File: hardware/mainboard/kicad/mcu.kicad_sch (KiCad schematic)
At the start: 8 parts, among them J15 J_EXP

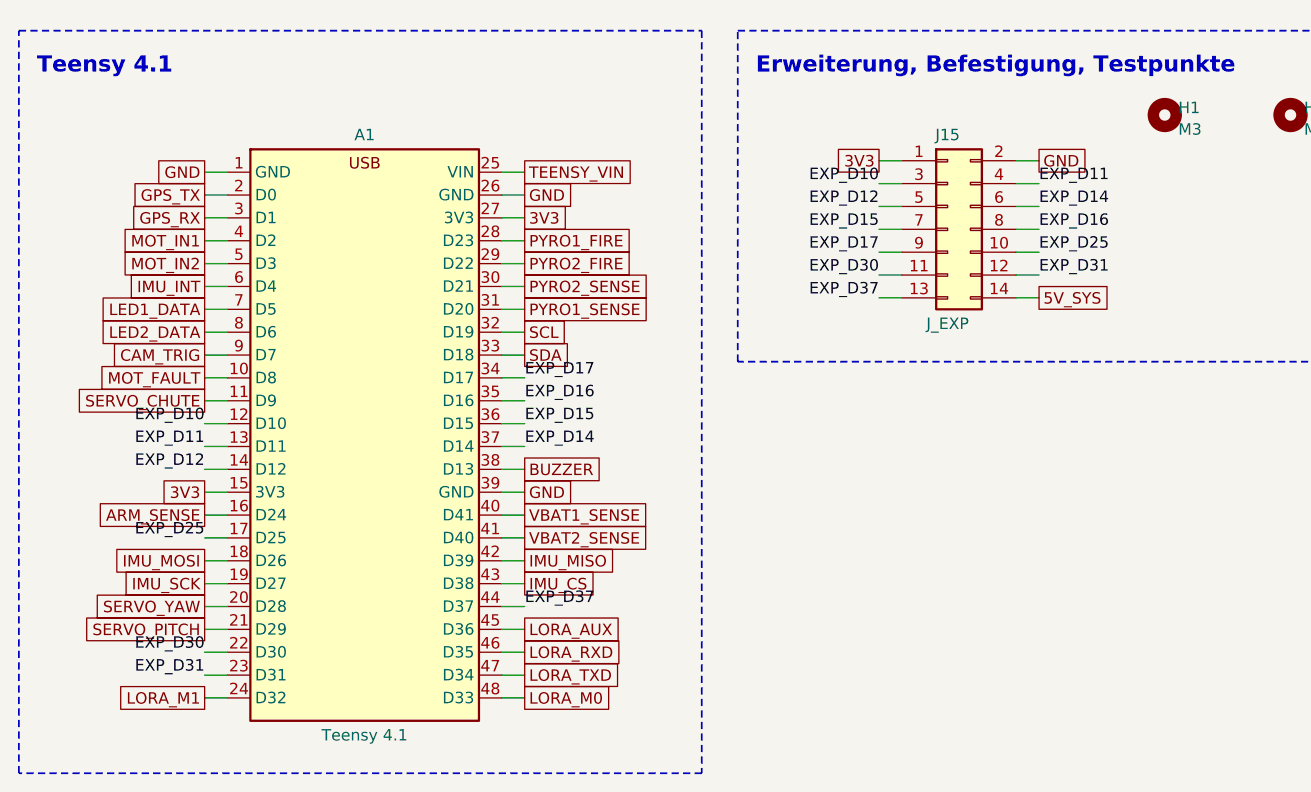
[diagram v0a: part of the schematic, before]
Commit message: Platine rev B geroutet: alle 134 Footprints platziert, DRC ohne Fehler, 3 offene Verbindungen; Renders und Lagenbilder; Fertigervergleich
- Lagen: In1 GND, B.Cu geteilte Versorgungsflaeche GND_PWR/5V_SYS, Plane-Vias an jedem SMD-Pad
- Freerouting 2.5.0 (JAR, Temurin 25) mit zwei Nachlaeufen auf fixierter Verdrahtung und kollisionsgeprueften Stummeln
- check_design.py: Netzliste gegen Spezifikation §4 (OK), make.sh fuer die ganze Kette
- 3D-Modelle Teensy 4.1 und XT30PW-M (CadQuery), Renders und layers.pdf in kicad/img
- Fertiger_2026-10-21.md: JLCPCB empfohlen, Aisler als EU-Rueckfall, BMP390 bei JLC nicht lieferbar
- naechster Schritt laut kicad/README.md §8: Review-Punkte A1-A5 (review_kicad_2026-10-21.md) vor dem Handrouting

Co-Authored-By: Claude Opus 5.5 <noreply@anthropic.com>
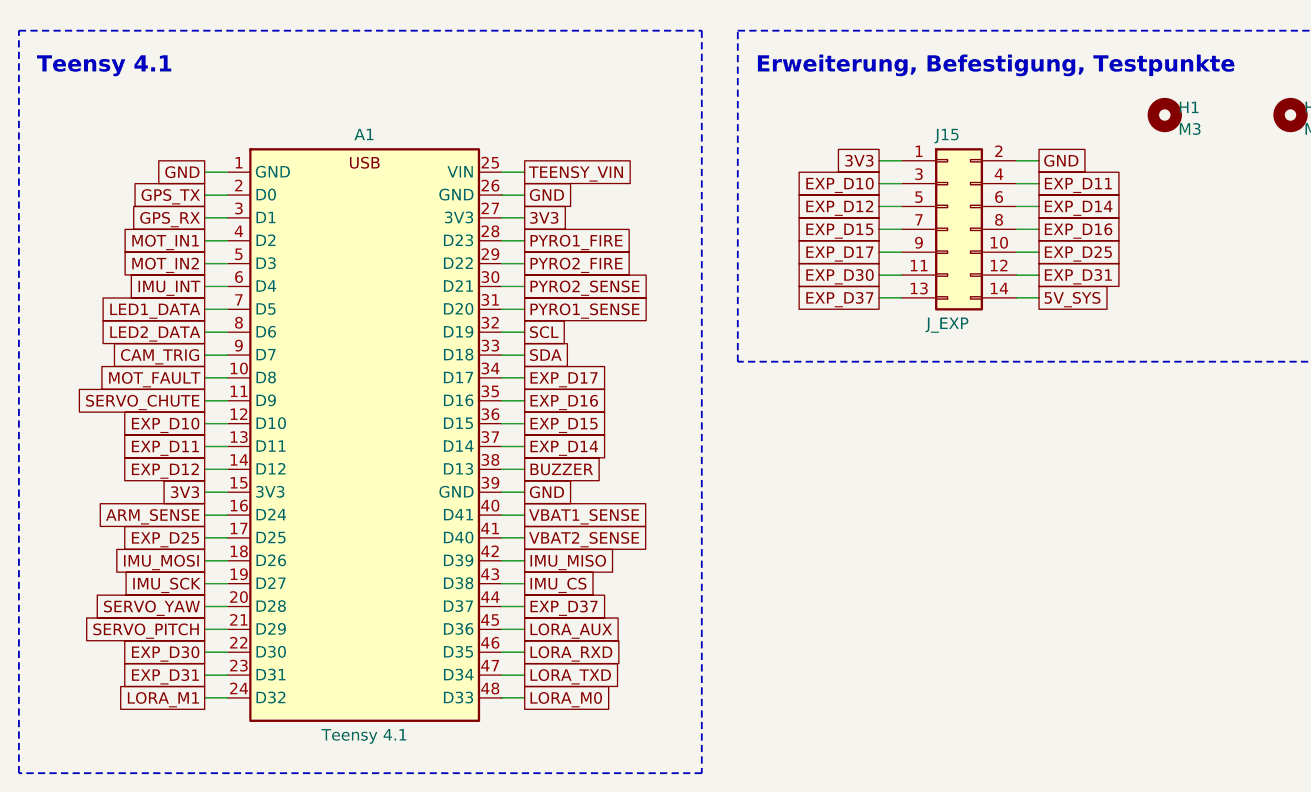
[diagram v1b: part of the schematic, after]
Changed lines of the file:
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@@
 		(company "Mission Space")
 		(comment 1 "Teensy 4.1 auf Buchsenleisten, Erweiterungsleiste, Befestigung")
-		(comment 2 "erzeugt von hardware/mainboard/kicad/gen_schematic.py aus circuit.py - nicht von Hand aendern")
+		(comment 2 "erzeugt aus circuit.py (gen_schematic.py)")
 	)
 	(text "Teensy 4.1 auf Buchsenleisten, Erweiterungsleiste, Befestigung"
@@
 		(stroke (width 0) (type default))
 	)
-	(label "EXP_D10"
+	(global_label "EXP_D10"
+		(shape passive)
 		(at 40.64 73.66 180)
 		(fields_autoplaced yes)
-		(effects (font (size 1.27 1.27)) (justify right bottom))
+		(effects (font (size 1.27 1.27)) (justify right))
 	)
 	(wire
@@
 		(stroke (width 0) (type default))
 	)
-	(label "EXP_D11"
+	(global_label "EXP_D11"
+		(shape passive)
 		(at 40.64 76.2 180)
 		(fields_autoplaced yes)
-		(effects (font (size 1.27 1.27)) (justify right bottom))
+		(effects (font (size 1.27 1.27)) (justify right))
 	)
 	(wire
@@
 		(stroke (width 0) (type default))
 	)
-	(label "EXP_D12"
+	(global_label "EXP_D12"
+		(shape passive)
 		(at 40.64 78.74 180)
 		(fields_autoplaced yes)
-		(effects (font (size 1.27 1.27)) (justify right bottom))
+		(effects (font (size 1.27 1.27)) (justify right))
 	)
 	(wire
@@
 		(stroke (width 0) (type default))
 	)
-	(label "EXP_D25"
+	(global_label "EXP_D25"
+		(shape passive)
 		(at 40.64 86.36 180)
 		(fields_autoplaced yes)
-		(effects (font (size 1.27 1.27)) (justify right bottom))
+		(effects (font (size 1.27 1.27)) (justify right))
 	)
 	(wire
@@
 		(stroke (width 0) (type default))
 	)
-	(label "EXP_D30"
+	(global_label "EXP_D30"
+		(shape passive)
 		(at 40.64 99.06 180)
 		(fields_autoplaced yes)
-		(effects (font (size 1.27 1.27)) (justify right bottom))
+		(effects (font (size 1.27 1.27)) (justify right))
 	)
 	(wire
@@
 		(stroke (width 0) (type default))
 	)
-	(label "EXP_D31"
+	(global_label "EXP_D31"
+		(shape passive)
 		(at 40.64 101.6 180)
 		(fields_autoplaced yes)
-		(effects (font (size 1.27 1.27)) (justify right bottom))
+		(effects (font (size 1.27 1.27)) (justify right))
 	)
 	(wire
@@
 		(stroke (width 0) (type default))
 	)
-	(label "EXP_D17"
+	(global_label "EXP_D17"
+		(shape passive)
 		(at 76.2 68.58 0)
 		(fields_autoplaced yes)
-		(effects (font (size 1.27 1.27)) (justify left bottom))
+		(effects (font (size 1.27 1.27)) (justify left))
 	)
 	(wire
@@
 		(stroke (width 0) (type default))
 	)
-	(label "EXP_D16"
+	(global_label "EXP_D16"
+		(shape passive)
 		(at 76.2 71.12 0)
 		(fields_autoplaced yes)
-		(effects (font (size 1.27 1.27)) (justify left bottom))
+		(effects (font (size 1.27 1.27)) (justify left))
 	)
 	(wire
@@
 		(stroke (width 0) (type default))
 	)
-	(label "EXP_D15"
+	(global_label "EXP_D15"
+		(shape passive)
 		(at 76.2 73.66 0)
 		(fields_autoplaced yes)
-		(effects (font (size 1.27 1.27)) (justify left bottom))
+		(effects (font (size 1.27 1.27)) (justify left))
 	)
 	(wire
@@
 		(stroke (width 0) (type default))
 	)
-	(label "EXP_D14"
+	(global_label "EXP_D14"
+		(shape passive)
 		(at 76.2 76.2 0)
 		(fields_autoplaced yes)
-		(effects (font (size 1.27 1.27)) (justify left bottom))
+		(effects (font (size 1.27 1.27)) (justify left))
 	)
 	(wire
@@
 		(stroke (width 0) (type default))
 	)
-	(label "EXP_D37"
+	(global_label "EXP_D37"
+		(shape passive)
 		(at 76.2 93.98 0)
 		(fields_autoplaced yes)
-		(effects (font (size 1.27 1.27)) (justify left bottom))
+		(effects (font (size 1.27 1.27)) (justify left))
 	)
 	(wire
@@
 		(stroke (width 0) (type default))
 	)
-	(label "EXP_D10"
+	(global_label "EXP_D10"
+		(shape passive)
 		(at 115.57 46.99 180)
 		(fields_autoplaced yes)
-		(effects (font (size 1.27 1.27)) (justify right bottom))
+		(effects (font (size 1.27 1.27)) (justify right))
 	)
 	(wire
@@
 		(stroke (width 0) (type default))
 	)
-	(label "EXP_D11"
+	(global_label "EXP_D11"
+		(shape passive)
 		(at 133.35 46.99 0)
 		(fields_autoplaced yes)
-		(effects (font (size 1.27 1.27)) (justify left bottom))
+		(effects (font (size 1.27 1.27)) (justify left))
 	)
 	(wire
@@
 		(stroke (width 0) (type default))
 	)
-	(label "EXP_D12"
+	(global_label "EXP_D12"
+		(shape passive)
 		(at 115.57 49.53 180)
 		(fields_autoplaced yes)
-		(effects (font (size 1.27 1.27)) (justify right bottom))
+		(effects (font (size 1.27 1.27)) (justify right))
 	)
 	(wire
@@
 		(stroke (width 0) (type default))
 	)
-	(label "EXP_D14"
+	(global_label "EXP_D14"
+		(shape passive)
 		(at 133.35 49.53 0)
 		(fields_autoplaced yes)
-		(effects (font (size 1.27 1.27)) (justify left bottom))
+		(effects (font (size 1.27 1.27)) (justify left))
 	)
 	(wire
@@
 		(stroke (width 0) (type default))
 	)
-	(label "EXP_D15"
+	(global_label "EXP_D15"
+		(shape passive)
 		(at 115.57 52.07 180)
 		(fields_autoplaced yes)
-		(effects (font (size 1.27 1.27)) (justify right bottom))
+		(effects (font (size 1.27 1.27)) (justify right))
 	)
 	(wire
@@
 		(stroke (width 0) (type default))
 	)
-	(label "EXP_D16"
+	(global_label "EXP_D16"
+		(shape passive)
 		(at 133.35 52.07 0)
 		(fields_autoplaced yes)
-		(effects (font (size 1.27 1.27)) (justify left bottom))
+		(effects (font (size 1.27 1.27)) (justify left))
 	)
 	(wire
@@
 		(stroke (width 0) (type default))
 	)
-	(label "EXP_D17"
+	(global_label "EXP_D17"
+		(shape passive)
 		(at 115.57 54.61 180)
 		(fields_autoplaced yes)
-		(effects (font (size 1.27 1.27)) (justify right bottom))
+		(effects (font (size 1.27 1.27)) (justify right))
 	)
 	(wire
@@
 		(stroke (width 0) (type default))
 	)
-	(label "EXP_D25"
+	(global_label "EXP_D25"
+		(shape passive)
 		(at 133.35 54.61 0)
 		(fields_autoplaced yes)
-		(effects (font (size 1.27 1.27)) (justify left bottom))
+		(effects (font (size 1.27 1.27)) (justify left))
 	)
 	(wire
@@
 		(stroke (width 0) (type default))
 	)
-	(label "EXP_D30"
+	(global_label "EXP_D30"
+		(shape passive)
 		(at 115.57 57.15 180)
 		(fields_autoplaced yes)
-		(effects (font (size 1.27 1.27)) (justify right bottom))
+		(effects (font (size 1.27 1.27)) (justify right))
 	)
 	(wire
@@
 		(stroke (width 0) (type default))
 	)
-	(label "EXP_D31"
+	(global_label "EXP_D31"
+		(shape passive)
 		(at 133.35 57.15 0)
 		(fields_autoplaced yes)
-		(effects (font (size 1.27 1.27)) (justify left bottom))
+		(effects (font (size 1.27 1.27)) (justify left))
 	)
 	(wire
@@
 		(stroke (width 0) (type default))
 	)
-	(label "EXP_D37"
+	(global_label "EXP_D37"
+		(shape passive)
 		(at 115.57 59.69 180)
 		(fields_autoplaced yes)
-		(effects (font (size 1.27 1.27)) (justify right bottom))
-	)
-	(wire
+		(effects (font (size 1.27 1.27)) (justify right))
+	)
+	(wire

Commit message: Kartonaut: Name, Missionsabzeichen, Bestückungsdruck neu, Lötstopp blau
- Projekt heißt Kartonaut (Karton + Astronaut); Flüge werden hochgezählt, Erstflug = Kartonaut 1
- Abzeichen als Polygone in hardware/mainboard/kicad/logo.py, SVGs in docs/brand/
- spacecode/ -> firmware/, Bodenstation-Repo groundcode -> kartonaut-ground (Links, .gitignore)
- gen_pcb.py silk: Bestückungsdruck nur neu setzen, auf der gerouteten Platine; 1,0 mm Schrift,
  freie Plätze statt Überlappungen, Kurznamen an den Steckern, Testpunkte mit Netznamen,
  kleines Abzeichen vorn; hinten Abzeichen 20 mm und Steckerbelegung
- Stackup JLC04161H-7628 mit blauem Lötstopp im Board, Renders mit Stackup-Farben
- DRC-Druckwarnungen 167 -> 14 (Rest aus Footprint-Umrissen)

Co-Authored-By: Claude Opus 5.5 <noreply@anthropic.com>
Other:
- company: Mission Space -> Kartonaut
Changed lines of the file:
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@@
 		(date "2026-10-21")
 		(rev "B")
-		(company "Mission Space")
+		(company "Kartonaut")
 		(comment 1 "Teensy 4.1 auf Buchsenleisten, Erweiterungsleiste, Befestigung")
 		(comment 2 "erzeugt aus circuit.py (gen_schematic.py)")

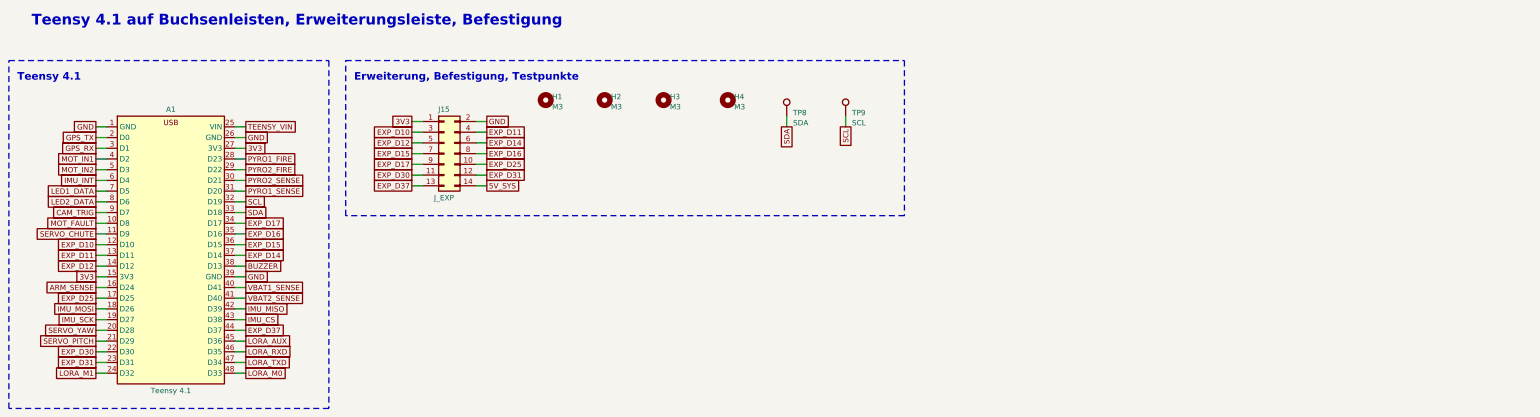
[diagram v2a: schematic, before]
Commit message: Mainboard rev B1: Review A1-A8 und Entscheidungen E1-E10 eingearbeitet, 2S-Pfad als F.Cu-Flaechen, 28 Verbindungen offen
Schaltung (circuit.py, ERC 0, Netzliste gegen README §4 OK): Hold-up hinter D1, EN-Teiler 330k/115k,
P-FET-Lastschalter je Akku, Polyfuse je Akku, Kelvin-Shunt mit INA239 an SPI1, BMP390 an SPI1,
74HC138/74HC4051 mit gemeinsamer Adresse, J_STACK 2x10 mit LDO 3V3_EXP, 1S-Lader MCP73831,
J_CHG2, vier Pyro-Kanaele (3/4 DNP), vierter Servo, alle Servos und Rollmotor an VSERVO,
3V3_SENS, eine WS2812B-Kette, Summer Pin 37, E22 NRST Pin 6; 166 Bauteile.

Platine (gen_pcb.py): neue Platzierung, 2S-Pfad, Pyro-Ausgaenge und VSYS_IN als F.Cu-Flaechen mit
Sperrflaechen fuer Freerouting, Strom-Klasse nur F.Cu, IMU-Zone 5 mm, patch mit Umweg ueber In2.
DRC 0 Fehler, Paritaet 0, kein 2S-Netz auf In2; 28 offene Verbindungen, Liste in kicad/README.md §5.5.
Spezifikation README.md und kicad/README.md auf B1 nachgezogen, review_check_layout.py fuer B1.

Co-Authored-By: Claude Opus 5.5 <noreply@anthropic.com>
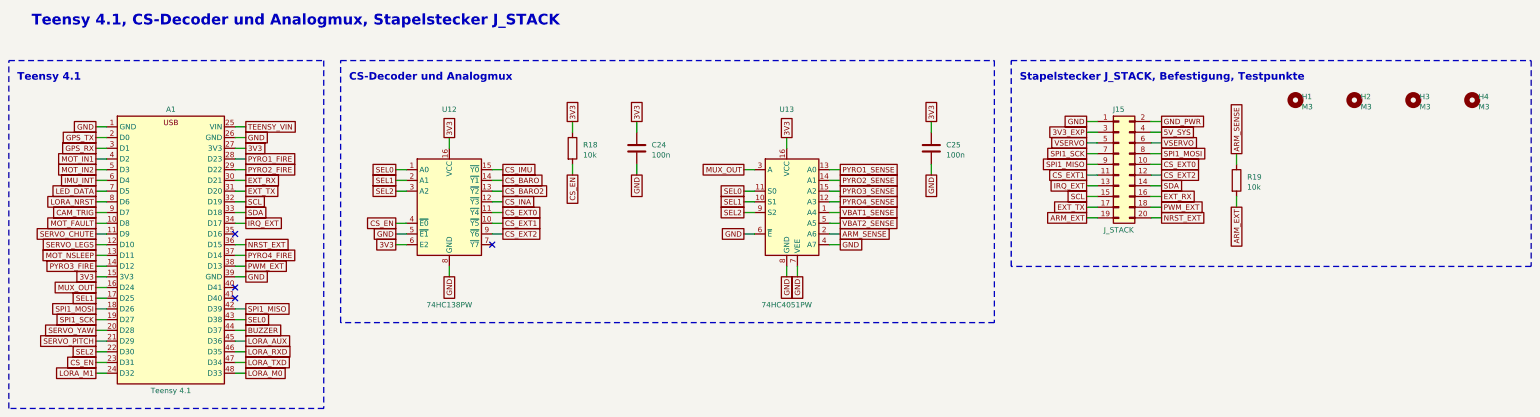
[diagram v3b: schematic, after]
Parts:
- removed TP8: SDA, TestPoint:TestPoint_Pad_D1.5mm, symbol Connector:TestPoint
- removed TP9: SCL, TestPoint:TestPoint_Pad_D1.5mm, symbol Connector:TestPoint
- added C24, C25: 100n, Capacitor_SMD:C_0603_1608Metric, symbol Device:C
- added R18, R19: 10k, Resistor_SMD:R_0603_1608Metric, symbol Device:R
- added U12: 74HC138PW, Package_SO:TSSOP-16_4.4x5mm_P0.65mm, symbol 74xx:74HC138
- added U13: 74HC4051PW, Package_SO:TSSOP-16_4.4x5mm_P0.65mm, symbol 74xx:74HC4051
- J15: value J_EXP -> J_STACK; footprint Connector_PinHeader_2.54mm:PinHeader_2x07_P2.54mm_Vertical -> Connector_PinHeader_2.54mm:PinHeader_2x10_P2.54mm_Vertical; symbol Connector_Generic:Conn_02x07_Odd_Even -> Connector_Generic:Conn_02x10_Odd_Even; Funktion J_EXP -> J_STACK
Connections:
- net 3V3: now also C24.1, C25.1, R18.1, U12.16 (VCC), U12.6 (E2), U13.16 (VCC); no longer J15.1 (Pin_1)
- net 5V_SYS: now also J15.4 (Pin_4); no longer J15.14 (Pin_14)
- net ARM_SENSE: now also R19.1, U13.2 (A6); no longer A1.16 (D24)
- net BUZZER: now also A1.44 (D37); no longer A1.38 (D13)
- net GND: now also J15.1 (Pin_1), C24.2, C25.2, U12.5 (~{E1}), U12.8 (GND), U13.4 (A7), U13.6 (~{E}), U13.7 (VEE), U13.8 (GND); no longer J15.2 (Pin_2)
- net PYRO1_SENSE: now also U13.13 (A0); no longer A1.31 (D20)
- net PYRO2_SENSE: now also U13.14 (A1); no longer A1.30 (D21)
- net SCL: now also J15.15 (Pin_15)
- net SDA: now also J15.14 (Pin_14)
- net VBAT1_SENSE: now also U13.1 (A4); no longer A1.40 (D41)
- net VBAT2_SENSE: now also U13.5 (A5); no longer A1.41 (D40)
- net EXP_D10 renamed 3V3_EXP
- net 3V3_EXP: no longer A1.12 (D10)
- net EXP_D11 renamed MOT_NSLEEP
- net MOT_NSLEEP: no longer J15.4 (Pin_4)
- net EXP_D12 renamed PYRO3_FIRE
- net PYRO3_FIRE: no longer J15.5 (Pin_5)
- net EXP_D14 renamed PYRO4_FIRE
- net PYRO4_FIRE: no longer J15.6 (Pin_6)
- net EXP_D15 renamed NRST_EXT
- net NRST_EXT: now also J15.20 (Pin_20); no longer J15.7 (Pin_7)
- net EXP_D16: no longer names the net of A1.35 (D16)
- net EXP_D16: no longer J15.8 (Pin_8)
- net EXP_D17 renamed IRQ_EXT
- net IRQ_EXT: now also J15.13 (Pin_13); no longer J15.9 (Pin_9)
- net EXP_D25 renamed CS_EXT0
- net CS_EXT0: now also U12.11 (~{Y4}); no longer A1.17 (D25)
- net EXP_D30 renamed CS_EXT1
- net CS_EXT1: now also U12.10 (~{Y5}); no longer A1.22 (D30)
- net EXP_D31 renamed CS_EN
- net CS_EN: now also R18.2, U12.4 (~{E0}); no longer J15.12 (Pin_12)
- removed net EXP_D37: A1.44 (D37), J15.13 (Pin_13)
- net IMU_CS renamed SEL0
- net SEL0: now also U12.1 (A0), U13.11 (S0)
- net IMU_MISO renamed SPI1_MISO
- net SPI1_MISO: now also J15.9 (Pin_9)
- net IMU_MOSI renamed SPI1_MOSI
- net SPI1_MOSI: now also J15.8 (Pin_8)
- net IMU_SCK renamed SPI1_SCK
- net SPI1_SCK: now also J15.7 (Pin_7)
- net LED1_DATA renamed LED_DATA
- net LED2_DATA renamed LORA_NRST
- new net ARM_EXT: J15.19 (Pin_19), R19.2
- new net CS_BARO: U12.14 (~{Y1})
- new net CS_BARO2: U12.13 (~{Y2})
- new net CS_EXT2: J15.12 (Pin_12), U12.9 (~{Y6})
- new net CS_IMU: U12.15 (~{Y0})
- new net CS_INA: U12.12 (~{Y3})
- new net EXT_RX: A1.30 (D21), J15.16 (Pin_16)
- new net EXT_TX: A1.31 (D20), J15.17 (Pin_17)
- new net GND_PWR: J15.2 (Pin_2)
- new net MUX_OUT: A1.16 (D24), U13.3 (A)
- new net PWM_EXT: A1.38 (D13), J15.18 (Pin_18)
- new net PYRO3_SENSE: U13.15 (A2)
- new net PYRO4_SENSE: U13.12 (A3)
- new net SEL1: A1.17 (D25), U12.2 (A1), U13.10 (S1)
- new net SEL2: A1.22 (D30), U12.3 (A2), U13.9 (S2)
- new net SERVO_LEGS: A1.12 (D10)
- new net VSERVO: J15.5 (Pin_5), J15.6 (Pin_6)
- no-connect marks 0 -> 4
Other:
- note added: "CS-Decoder und Analogmux"
- note added: "Stapelstecker J_STACK, Befestigung, Testpunkte"
- note added: "Teensy 4.1, CS-Decoder und Analogmux, Stapelstecker J_STACK"
- note removed: "Erweiterung, Befestigung, Testpunkte"
- note removed: "Teensy 4.1 auf Buchsenleisten, Erweiterungsleiste, Befestigung"
- moved on the sheet: H1, H2, H3, H4
